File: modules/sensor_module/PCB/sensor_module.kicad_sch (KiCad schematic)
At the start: 61 parts, among them J1 Screw_Terminal_01x02, J2 Conn_01x06_Socket, J3 Conn_01x03_Socket, SW1 SW_SPDT, U1 AMS1117-3.3, U2 AMS1117-5, U3 ESP-12E, U4 LM393, U5 MQ-5, U6 LM393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

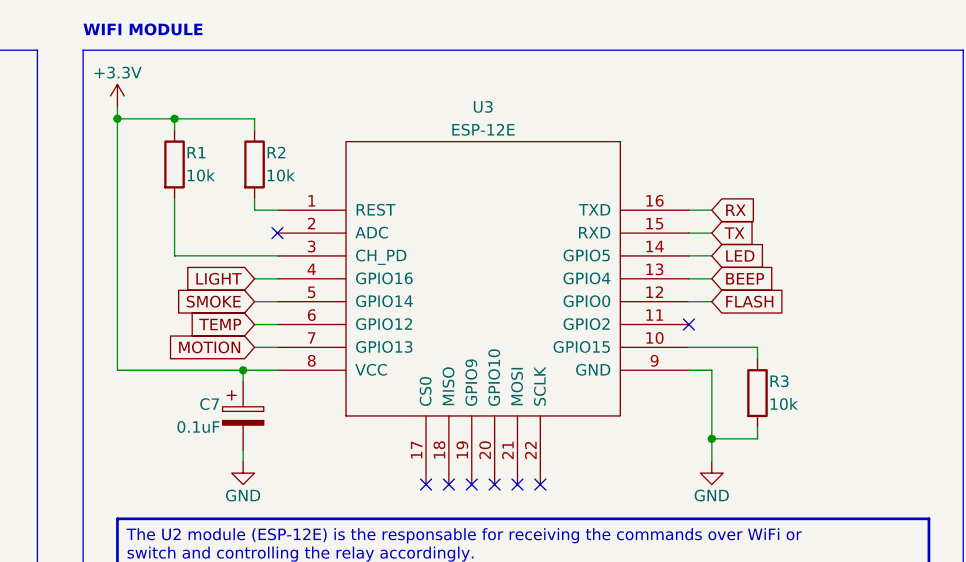
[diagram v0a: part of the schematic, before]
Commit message: Sensor module PCB layout finished
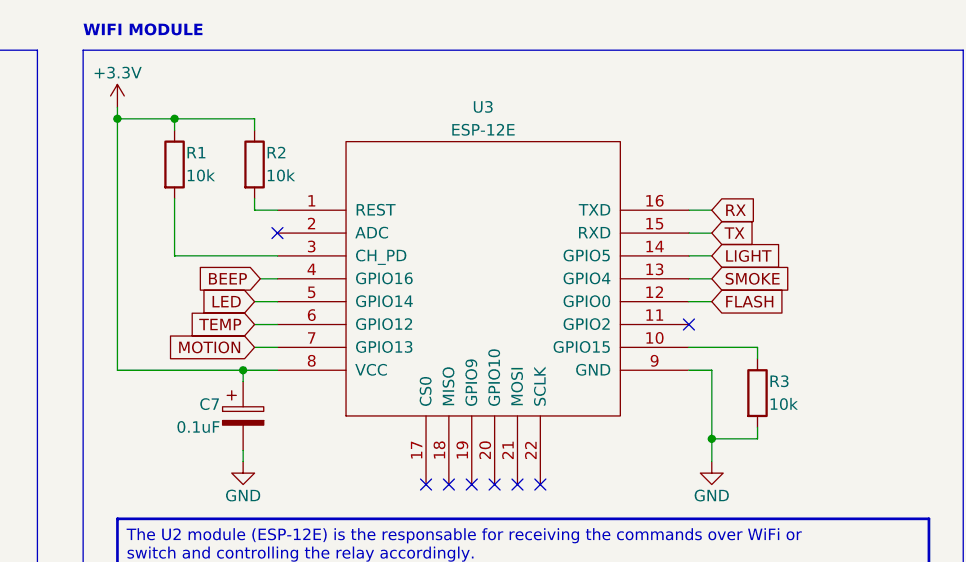
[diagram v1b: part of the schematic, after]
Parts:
- D2: footprint LED_SMD:LED_0603_1608Metric -> LED_THT:LED_D3.0mm; Color Green -> Red
- D3, D4, D5: Color Green -> Blue
- POT1, POT2, POT3, POT4: footprint Potentiometer_THT:Potentiometer_Bourns_3296W_Vertical -> MyLibrary:TRIM_3362P-1-103
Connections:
- net BEEP: now also U3.4 (GPIO16); no longer U3.13 (GPIO4)
- net LED: now also U3.5 (GPIO14); no longer U3.14 (GPIO5)
- net LIGHT: now also U3.14 (GPIO5); no longer U3.4 (GPIO16)
- net SMOKE: now also U3.13 (GPIO4); no longer U3.5 (GPIO14)
